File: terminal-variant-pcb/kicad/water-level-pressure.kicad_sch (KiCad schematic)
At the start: 38 parts, among them J1 Conn_01x03, J3 Conn_01x02, T1 TestPoint, T10 TestPoint, T11 TestPoint, T12 TestPoint, T13 TestPoint, T14 TestPoint, T15 TestPoint, T16 TestPoint, T17 TestPoint, T18 TestPoint, T19 TestPoint, T2 TestPoint, T20 TestPoint, T21 TestPoint, T22 TestPoint, T23 TestPoint, T24 TestPoint, T25 TestPoint, T26 TestPoint, T27 TestPoint, T28 TestPoint, T29 TestPoint, T3 TestPoint, T30 TestPoint, T4 TestPoint, T5 TestPoint, T6 TestPoint, T7 TestPoint, T8 TestPoint, T9 TestPoint

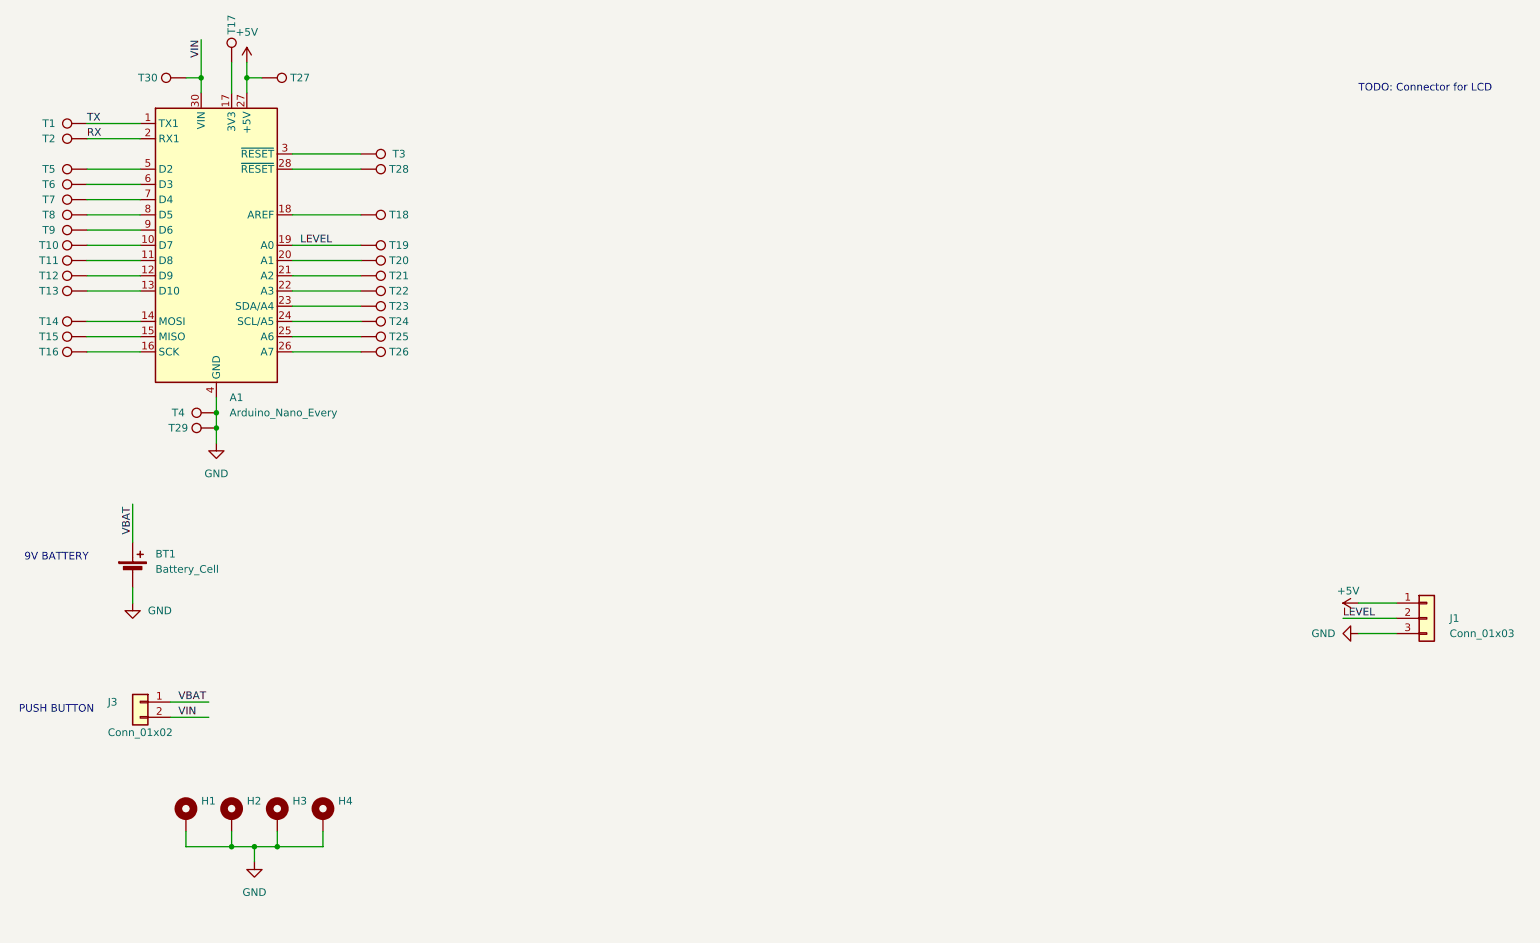
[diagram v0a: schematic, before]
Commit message: Add LCD connector. First draft. Update PDF schematic. Remove old SVG schematic.
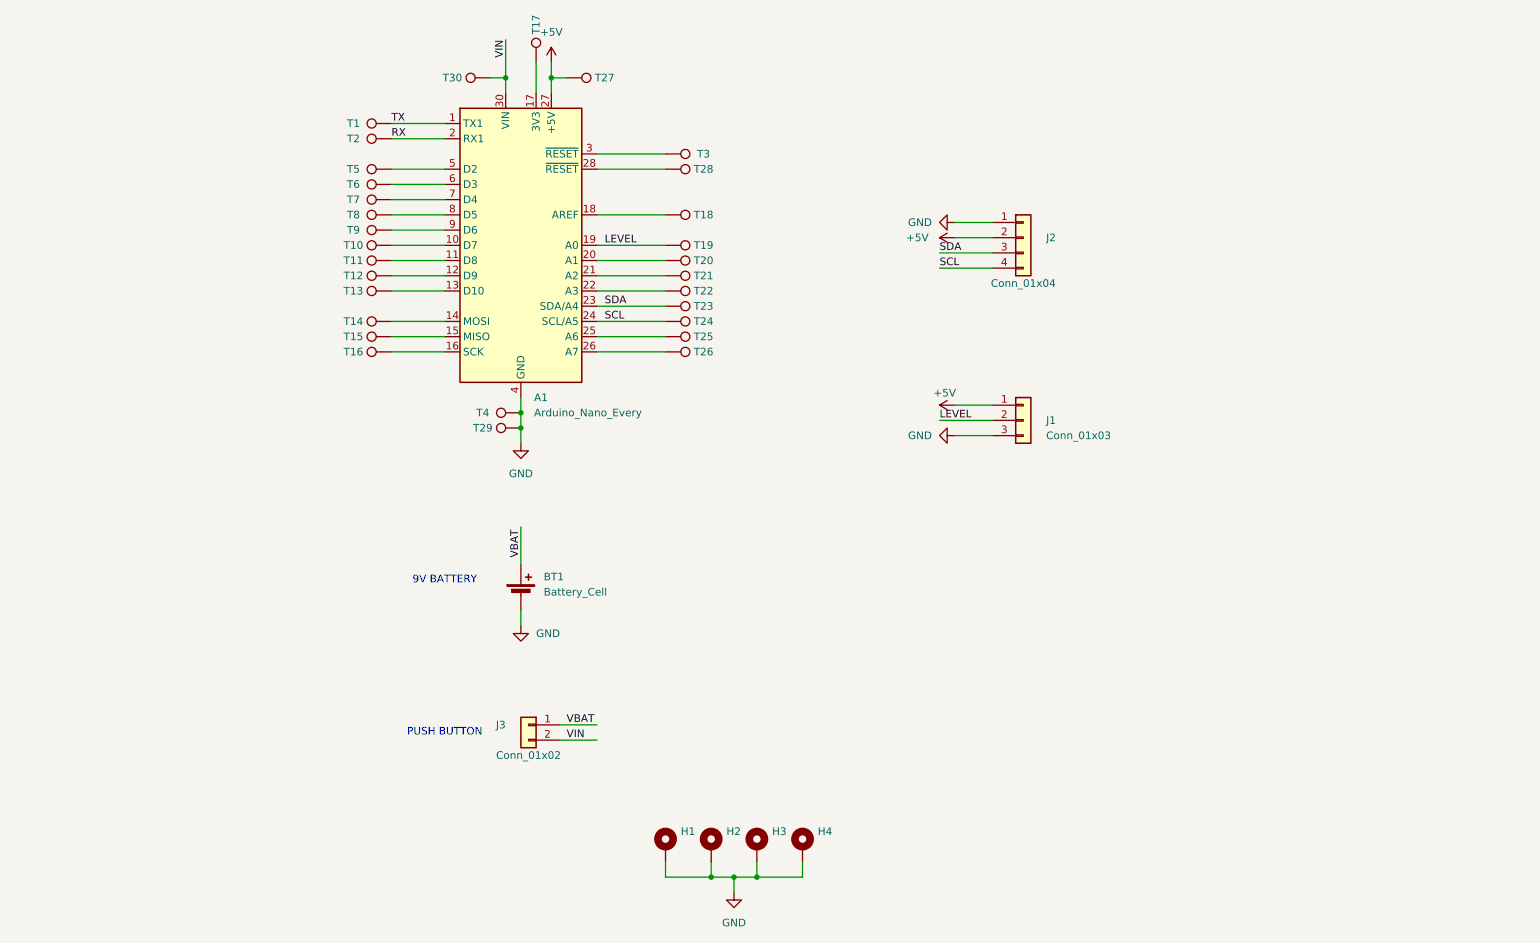
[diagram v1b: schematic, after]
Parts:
- added J2: Conn_01x04, Connector_PinHeader_2.54mm:PinHeader_1x04_P2.54mm_Vertical_SMD_Pin1Left, symbol Connector_Generic:Conn_01x04
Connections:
- net +5V: now also J2.2 (Pin_2)
- net GND: now also J2.1 (Pin_1)
- net SCL: now reaches A1.24 (SCL/A5), T24.1
- net SCL: now also J2.4 (Pin_4)
- net SDA: now reaches A1.23 (SDA/A4), T23.1
- net SDA: now also J2.3 (Pin_3)
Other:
- note removed: "TODO: Connector for LCD"
- moved on the sheet: A1, BT1, H1, H2, H3, H4, J1, J3, T1, T10, T11, T12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

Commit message: Add terminal block for sensor and update price.
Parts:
- BT1: LCSC (none) -> C5556545
- J1: LCSC (none) -> C691850
- J2: LCSC (none) -> C5160787
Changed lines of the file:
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@@
+			)
+		)
+		(property "LCSC" "C691850"
+			(at 190.5 106.68 0)
+			(effects
+				(font
+					(size 1.27 1.27)
+				)
+				(hide yes)
 			)
 		)
@@
 			)
 		)
+		(property "LCSC" "C5556545"
+			(at 106.68 132.7784 0)
+			(effects
+				(font
+					(size 1.27 1.27)
+				)
+				(hide yes)
+			)
+		)
 		(pin "2"
 		)
@@
 			)
 		)
+		(property "LCSC" "C5160787"
+			(at 190.5 76.2 0)
+			(effects
+				(font
+					(size 1.27 1.27)
+				)
+				(hide yes)
+			)
+		)

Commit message: Add terminal block for puch button and update price.
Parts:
- J3: LCSC (none) -> C699496
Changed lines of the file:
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@@
+			)
+		)
+		(property "LCSC" "C699496"
+			(at 100.33 157.48 0)
+			(effects
+				(font
+					(size 1.27 1.27)
+				)
+				(hide yes)
 			)
 		)

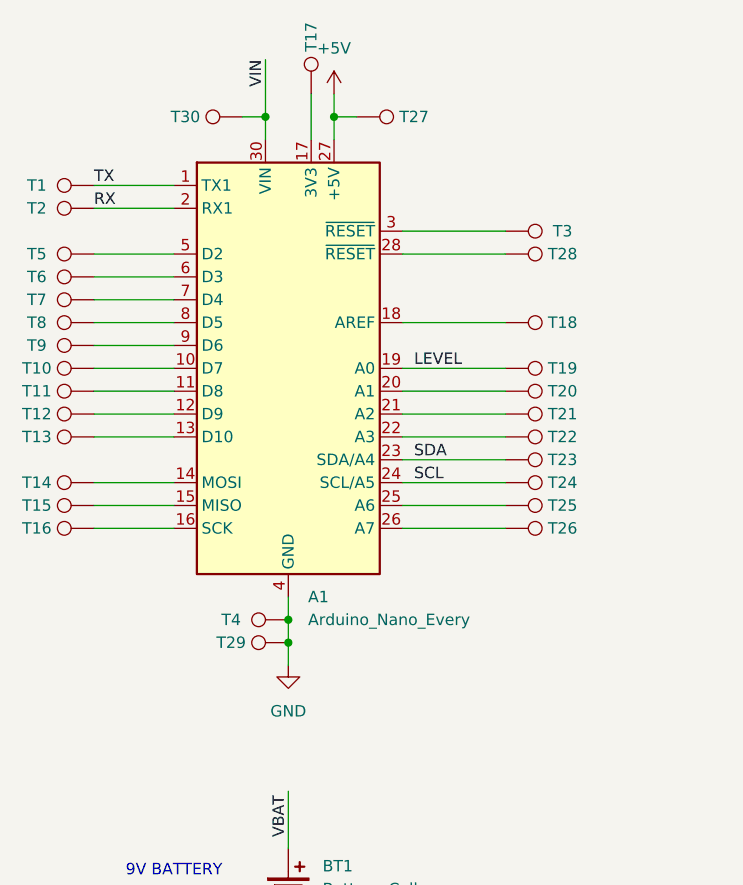
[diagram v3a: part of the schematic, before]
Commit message: Replacing Arduino footprint by pair of connectors footprints.
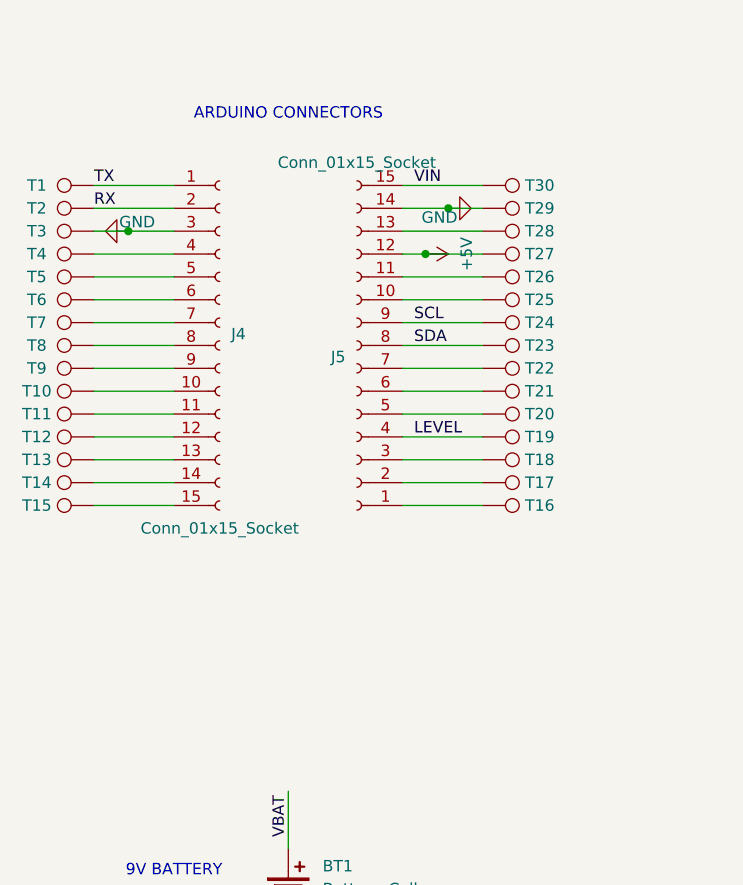
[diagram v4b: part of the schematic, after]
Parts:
- removed A1: Arduino_Nano_Every, Module:Arduino_Nano, symbol MCU_Module:Arduino_Nano_Every
- added J4, J5: Conn_01x15_Socket, Connector_PinSocket_2.54mm:PinSocket_1x15_P2.54mm_Vertical, symbol Connector:Conn_01x15_Socket
- BT1: now left out of the parts list
- H1, H2, H3, H4, T1, T10, T11, T12, T13, T14, T15, T16, T17, T18, T19, T2, T20, T21, T22, T23, T24, T25, T26, T27, T28, T29, T3, T30, T4, T5, T6, T7, T8, T9: Field4 (none) -> ${REFERENCE}; now left out of the parts list
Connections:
- net +5V: now also J5.12 (Pin_12)
- net GND: now also T3.1, J4.3 (Pin_3), J5.14 (Pin_14); no longer T4.1
- net LEVEL: now also J5.4 (Pin_4)
- net RX: now also J4.2 (Pin_2)
- net SCL: now also J5.9 (Pin_9)
- net SDA: now also J5.8 (Pin_8)
- net TX: now also J4.1 (Pin_1)
- net VIN: now also J5.15 (Pin_15)
- net at T6.1: now also J4.6 (Pin_6)
- net at T18.1: now also J5.3 (Pin_3)
- net at T7.1: now also J4.7 (Pin_7)
- net at T17.1: now also J5.2 (Pin_2)
- net at T15.1: now also J4.15 (Pin_15)
- net at T25.1: now also J5.10 (Pin_10)
- net at T5.1: now also J4.5 (Pin_5)
- net at T20.1: now also J5.5 (Pin_5)
- net at T16.1: now also J5.1 (Pin_1)
- net at T9.1: now also J4.9 (Pin_9)
- net at T8.1: now also J4.8 (Pin_8)
- net at T12.1: now also J4.12 (Pin_12)
- net at T28.1: now also J5.13 (Pin_13)
- net at T11.1: now also J4.11 (Pin_11)
- net at T26.1: now also J5.11 (Pin_11)
- net at T10.1: now also J4.10 (Pin_10)
- net at T13.1: now also J4.13 (Pin_13)
- net at T14.1: now also J4.14 (Pin_14)
- net at T21.1: now also J5.6 (Pin_6)
- net at T22.1: now also J5.7 (Pin_7)
- new net: J4.4 (Pin_4), T4.1
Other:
- note added: "ARDUINO CONNECTORS"
- moved on the sheet: T10, T11, T12, T13, T17, T18, T19, T20, T21, T22, T23, T24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

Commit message: Remove the only SMD component to avoid cost.
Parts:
- J2: footprint Connector_PinHeader_2.54mm:PinHeader_1x04_P2.54mm_Vertical_SMD_Pin1Left -> Connector_PinHeader_2.54mm:PinHeader_1x04_P2.54mm_Vertical; LCSC C5160787 -> C124378
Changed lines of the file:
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@@
 			)
 		)
-		(property "Footprint" "Connector_PinHeader_2.54mm:PinHeader_1x04_P2.54mm_Vertical_SMD_Pin1Left"
+		(property "Footprint" "Connector_PinHeader_2.54mm:PinHeader_1x04_P2.54mm_Vertical"
 			(at 186.69 76.2 0)
 			(hide yes)
@@
 			)
 		)
-		(property "LCSC" "C5160787"
+		(property "LCSC" "C124378"
 			(at 190.5 76.2 0)
 			(hide yes)

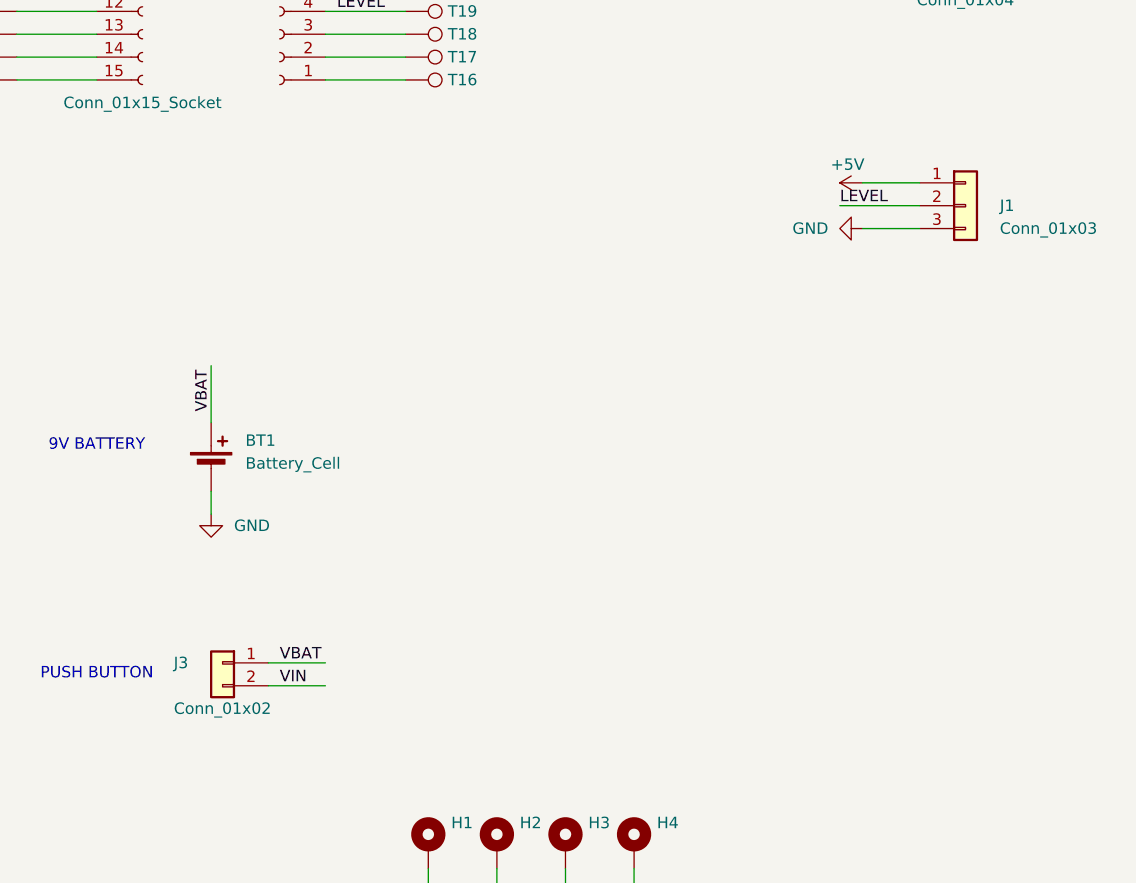
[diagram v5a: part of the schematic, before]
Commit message: Version 0.5. Fix connectors orientation. Fix title in schematic (was title of old version using ultrasonic). Fix pads footprints paths (was old ultrasonic).
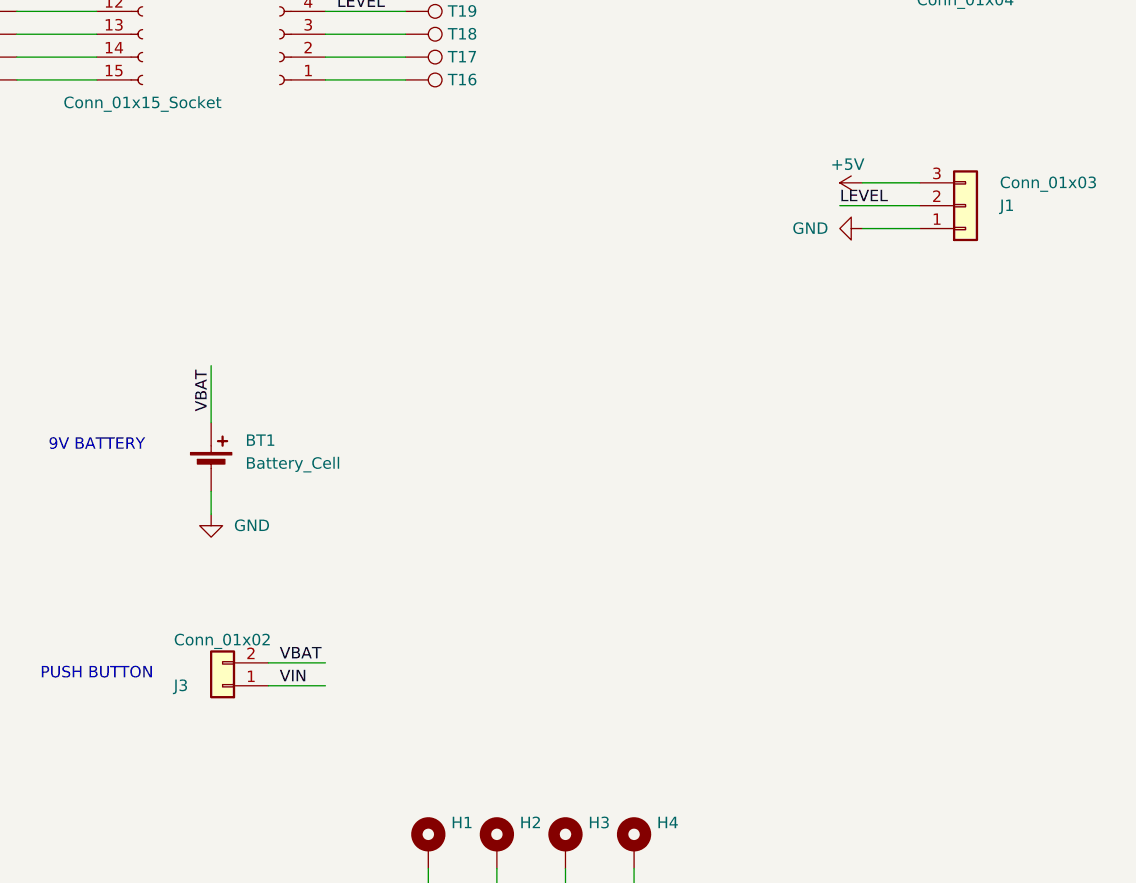
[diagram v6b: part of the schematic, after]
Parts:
- T1, T10, T11, T12, T13, T14, T15, T16, T17, T18, T19, T2, T20, T21, T22, T23, T24, T25, T26, T27, T28, T29, T3, T30, T4, T5, T6, T7, T8, T9: footprint ultrasonic-pcb:TestPoint_THTPad_D1.6mm_Drill1.0mm_Variant -> water-level-pressure:TestPoint_THTPad_D1.6mm_Drill1.0mm_Variant
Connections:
- net +5V: now also J1.3 (Pin_3); no longer J1.1 (Pin_1)
- net GND: now also J1.1 (Pin_1); no longer J1.3 (Pin_3)
- net VBAT: now also J3.2 (Pin_2); no longer J3.1 (Pin_1)
- net VIN: now also J3.1 (Pin_1); no longer J3.2 (Pin_2)
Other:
- title: Ultrasonic sensor board 3.0 -> Water level sensor 0.5

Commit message: Fix schematic and PCB connection mistake.
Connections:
- net GND: now also J4.4 (Pin_4), T4.1; no longer J4.3 (Pin_3), T3.1
- net RESET_2: now reaches J5.13 (Pin_13), T28.1
- new net RESET_1: J4.3 (Pin_3), T3.1
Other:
- title: Water level sensor 0.5 -> Water level sensor 0.6
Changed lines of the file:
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@@
 	(paper "A4")
 	(title_block
-		(title "Water level sensor 0.5")
+		(title "Water level sensor 0.6")
 		(company "F4INX")
 	)
@@
 	)
 	(junction
-		(at 85.09 62.23)
+		(at 88.9 64.77)
 		(diameter 0)
 		(color 0 0 0 0)
@@
 	(wire
 		(pts
-			(xy 81.28 62.23) (xy 85.09 62.23)
-		)
-		(stroke
-			(width 0)
-			(type default)
-		)
-	)
-	(wire
-		(pts
 			(xy 115.57 69.85) (xy 124.46 69.85)
 		)
@@
 	(wire
 		(pts
+			(xy 88.9 64.77) (xy 90.17 64.77)
+		)
+		(stroke
+			(width 0)
+			(type default)
+		)
+	)
+	(wire
+		(pts
 			(xy 90.17 85.09) (xy 81.28 85.09)
 		)
@@
 	(wire
 		(pts
-			(xy 81.28 64.77) (xy 90.17 64.77)
+			(xy 81.28 64.77) (xy 88.9 64.77)
 		)
 		(stroke
@@
 	(wire
 		(pts
-			(xy 85.09 62.23) (xy 90.17 62.23)
+			(xy 81.28 62.23) (xy 90.17 62.23)
 		)
 		(stroke
@@
 		)
 	)
+	(label "RESET_2"
+		(at 116.84 62.23 0)
+		(effects
+			(font
+				(size 1.27 1.27)
+			)
+			(justify left bottom)
+		)
+	)
 	(label "RX"
 		(at 81.28 59.69 0)
@@
 		)
 	)
+	(label "RESET_1"
+		(at 81.28 62.23 0)
+		(effects
+			(font
+				(size 1.27 1.27)
+			)
+			(justify left bottom)
+		)
+	)
 	(label "SDA"
 		(at 172.72 78.74 0)
@@
 	)
 	(symbol
+		(lib_id "power:GND")
+		(at 88.9 64.77 270)
+		(unit 1)
+		(body_style 1)
+		(exclude_from_sim no)
+		(in_bom yes)
+		(on_board yes)
+		(in_pos_files yes)
+		(dnp no)
+		(property "Reference" "#PWR08"
+			(at 82.55 64.77 0)
+			(hide yes)
+			(show_name no)
+			(do_not_autoplace no)
+			(effects
+				(font
+					(size 1.27 1.27)
+				)
+			)
+		)
+		(property "Value" "GND"
+			(at 81.28 63.754 90)
+			(show_name no)
+			(do_not_autoplace no)
+			(effects
+				(font
+					(size 1.27 1.27)
+				)
+				(justify left)
+			)
+		)
+		(property "Footprint" ""
+			(at 88.9 64.77 0)
+			(hide yes)
+			(show_name no)
+			(do_not_autoplace no)
+			(effects
+				(font
+					(size 1.27 1.27)
+				)
+			)
+		)
+		(property "Datasheet" ""
+			(at 88.9 64.77 0)
+			(hide yes)
+			(show_name no)
+			(do_not_autoplace no)
+			(effects
+				(font
+					(size 1.27 1.27)
+				)
+			)
+		)
+		(property "Description" ""
+			(at 88.9 64.77 0)
+			(show_name no)
+			(do_not_autoplace no)
+			(effects
+				(font
+					(size 1.27 1.27)
+				)
+			)
+		)
+		(pin "1"
+		)
+		(instances
+			(project "water-level-pressure"
+				(path "/33d3a90e-7f26-4b1c-8a5f-63dc17339015"
+					(reference "#PWR08")
+					(unit 1)
+				)
+			)
+		)
+	)
+	(symbol
 		(lib_id "power:+5V")
 		(at 175.26 104.14 90)
@@
 	)
 	(symbol
-		(lib_id "power:GND")
-		(at 85.09 62.23 270)
-		(unit 1)
-		(body_style 1)
-		(exclude_from_sim no)
-		(in_bom yes)
-		(on_board yes)
-		(in_pos_files yes)
-		(dnp no)
-		(property "Reference" "#PWR05"
-			(at 78.74 62.23 0)
-			(hide yes)
-			(show_name no)
-			(do_not_autoplace no)
-			(effects
-				(font
-					(size 1.27 1.27)
-				)
-			)
-		)
-		(property "Value" "GND"
-			(at 84.074 61.214 90)
-			(show_name no)
-			(do_not_autoplace no)
-			(effects
-				(font
-					(size 1.27 1.27)
-				)
-				(justify left)
-			)
-		)
-		(property "Footprint" ""
-			(at 85.09 62.23 0)
-			(hide yes)
-			(show_name no)
-			(do_not_autoplace no)
-			(effects
-				(font
-					(size 1.27 1.27)
-				)
-			)
-		)
-		(property "Datasheet" ""
-			(at 85.09 62.23 0)
-			(hide yes)
-			(show_name no)
-			(do_not_autoplace no)
-			(effects
-				(font
-					(size 1.27 1.27)
-				)
-			)
-		)
-		(property "Description" ""
-			(at 85.09 62.23 0)
-			(show_name no)
-			(do_not_autoplace no)
-			(effects
-				(font
-					(size 1.27 1.27)
-				)
-			)
-		)
-		(pin "1"
-		)
-		(instances
-			(project "water-level-pressure"
-				(path "/33d3a90e-7f26-4b1c-8a5f-63dc17339015"
-					(reference "#PWR05")
-					(unit 1)
-				)
-			)
-		)
-	)
-	(symbol
 		(lib_id "Connector:TestPoint")
 		(at 124.46 64.77 270)
@@
 		)
 		(property "Value" "GND"
-			(at 121.666 60.706 90)
+			(at 120.904 58.674 90)
 			(show_name no)
 			(do_not_autoplace no)
